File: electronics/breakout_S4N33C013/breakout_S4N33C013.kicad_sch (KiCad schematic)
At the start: 1 part

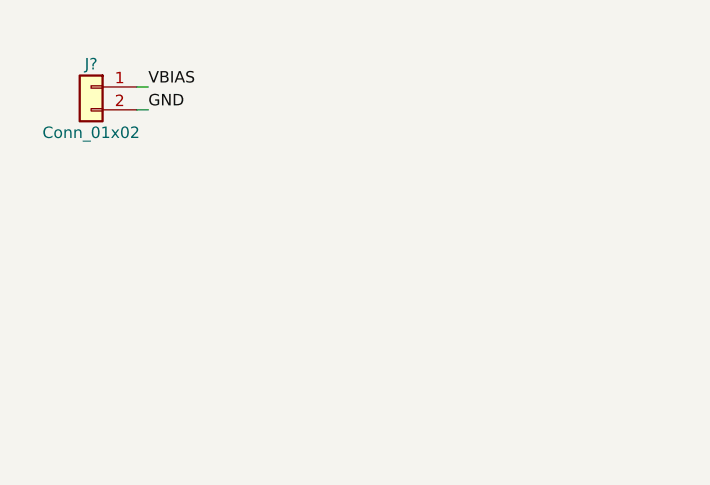
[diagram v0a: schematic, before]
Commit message: Started initial layout for breakout
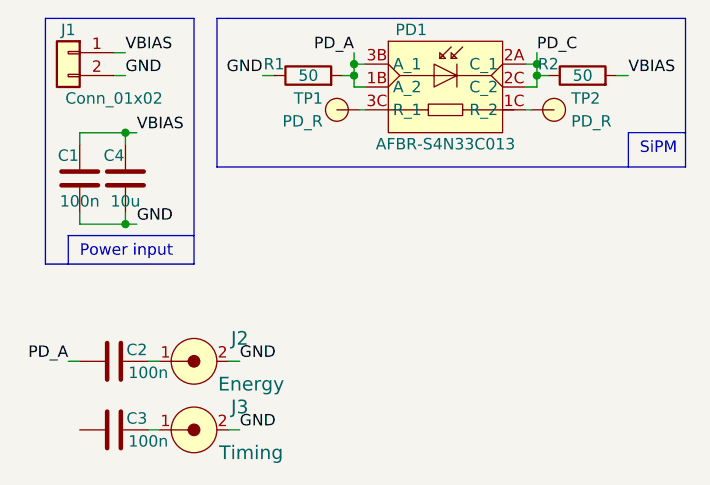
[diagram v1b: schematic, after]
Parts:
- added C1, C2, C3: 100n, SquantorRcl:C_0402, symbol Device:C
- added C4: 10u, SquantorRcl:C_1206, symbol Device:C
- added J2: Energy, SquantorConnectors:SMA_edge_6mm2, symbol SquantorConnectors:Coax
- added J3: Timing, SquantorConnectors:SMA_edge_6mm2, symbol SquantorConnectors:Coax
- added PD1: AFBR-S4N33C013, SquantorOpto:AFBR-S4N33C013, symbol SquantorOpto:AFBR-S4N33C013
- added R1, R2: 50, SquantorRcl:R_0603, symbol Device:R
- added TP1, TP2: PD_R, SquantorTestPoints:TestPoint_pad_circle_D05, symbol SquantorProto:testpad
- gave numbers to parts that had none: 1
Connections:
- net GND: now also C1.1, C4.1, J2.2, J3.2, R1.1
- net VBIAS: now also C1.2, C4.2, R2.2
- new net: C3.1, J3.1
- new net: PD1.3C (R_1), TP1.1
- new net: C2.1, J2.1
- new net: PD1.1C (R_2), TP2.1
- new net PD_A: C2.2, PD1.1B (A_2), PD1.3B (A_1), R1.2
- new net PD_C: PD1.2A (C_1), PD1.2C (C_2), R2.1
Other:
- note added: "Power input"
- note added: "SiPM"
- moved on the sheet: J1
